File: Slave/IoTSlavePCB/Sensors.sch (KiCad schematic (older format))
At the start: 4 parts, among them U5 SHTC3

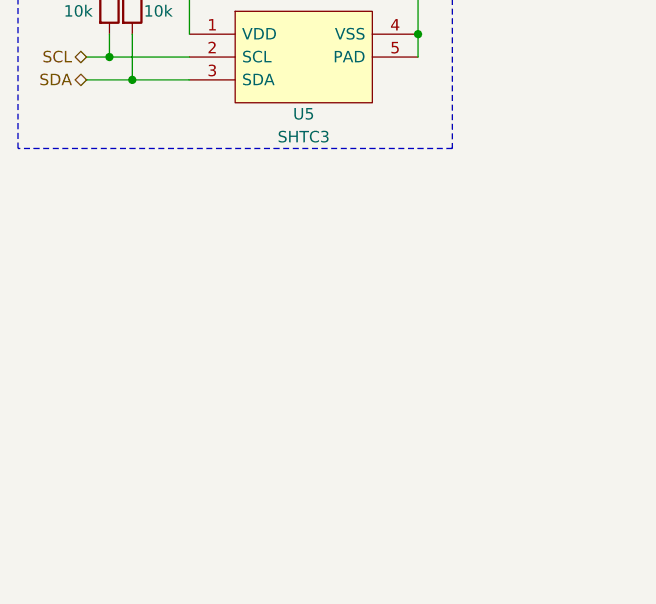
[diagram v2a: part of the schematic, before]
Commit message: Added battery voltage measurement circuit. Optimizations to antenna and general component placement.
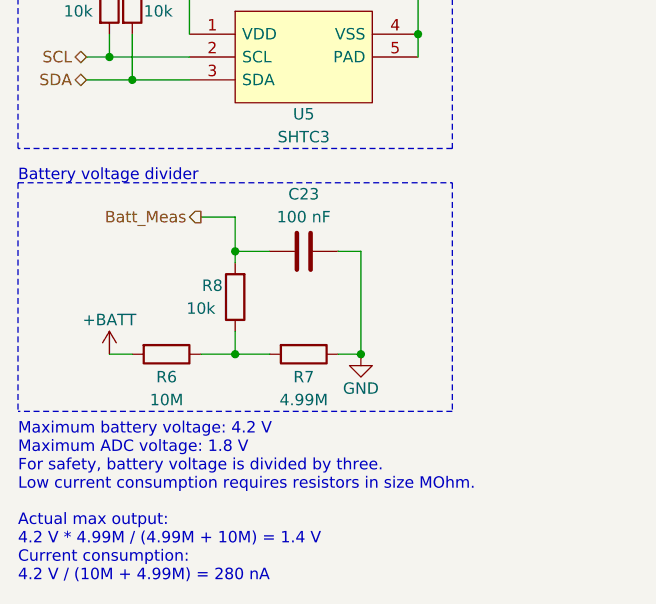
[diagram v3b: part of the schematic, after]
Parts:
- added C23: 100 nF, Capacitor_SMD:C_0603_1608Metric, symbol Device:C
- added R6: 10M, Resistor_SMD:R_0603_1608Metric, symbol Device:R
- added R7: 4.99M, Resistor_SMD:R_0603_1608Metric, symbol Device:R
- added R8: 10k, Resistor_SMD:R_0603_1608Metric, symbol Device:R
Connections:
- net GND: now also C23.1, R7.1
- new net: R6.1, R7.2, R8.1
- new net +BATT: R6.2
- new net Batt_Meas: C23.2, R8.2
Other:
- note added: "Actual max output:\n4.2 V * 4.99M / (4.99M + 10M) = 1.4 V\nCurrent consumption:\n4.2 V / (10M + 4.99M) = 280 nA"
- note added: "Battery voltage divider"
- note added: "Maximum battery voltage: 4.2 V\nMaximum ADC voltage: 1.8 V\nFor safety, battery voltage is divided by three.\nLow current consumption requires resistors in size MOhm."
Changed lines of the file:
@@
 Text Notes 4500 3100 0    50   ~ 0
 Temperature and humidity sensor
+$Comp
+L power:+BATT #PWR063
+U 1 1 5FC228FA
+P 4900 5200
+F 0 "#PWR063" H 4900 5050 50  0001 C CNN
+F 1 "+BATT" H 4900 5350 50  0000 C CNN
+F 2 "" H 4900 5200 50  0001 C CNN
+F 3 "" H 4900 5200 50  0001 C CNN
+	1    4900 5200
+	1    0    0    -1
+$EndComp
+$Comp
+L Device:R R6
+U 1 1 5FC2324E
+P 5150 5200
+F 0 "R6" V 5250 5200 50  0000 C CNN
+F 1 "10M" V 5350 5200 50  0000 C CNN
+F 2 "Resistor_SMD:R_0603_1608Metric" V 5080 5200 50  0001 C CNN
+F 3 "~" H 5150 5200 50  0001 C CNN
+	1    5150 5200
+	0    1    1    0
+$EndComp
+$Comp
+L Device:R R7
+U 1 1 5FC23C04
+P 5750 5200
+F 0 "R7" V 5850 5200 50  0000 C CNN
+F 1 "4.99M" V 5950 5200 50  0000 C CNN
+F 2 "Resistor_SMD:R_0603_1608Metric" V 5680 5200 50  0001 C CNN
+F 3 "~" H 5750 5200 50  0001 C CNN
+	1    5750 5200
+	0    1    1    0
+$EndComp
+Wire Wire Line
+	4900 5200 5000 5200
+Wire Wire Line
+	5900 5200 6000 5200
+$Comp
+L power:GND #PWR064
+U 1 1 5FC257F4
+P 6000 5200
+F 0 "#PWR064" H 6000 4950 50  0001 C CNN
+F 1 "GND" H 6000 5050 50  0000 C CNN
+F 2 "" H 6000 5200 50  0001 C CNN
+F 3 "" H 6000 5200 50  0001 C CNN
+	1    6000 5200
+	1    0    0    -1
+$EndComp
+Text HLabel 5300 4600 0    50   Output ~ 0
+Batt_Meas
+Wire Notes Line
+	4500 4450 6400 4450
+Text Notes 4500 4450 0    50   ~ 0
+Battery voltage divider
+Text Notes 4500 5800 0    50   ~ 0
+Maximum battery voltage: 4.2 V\nMaximum ADC voltage: 1.8 V\nFor safety, battery voltage is divided by three.\nLow current consumption requires resistors in size MOhm.
+Text Notes 4500 6200 0    50   ~ 0
+Actual max output:\n4.2 V * 4.99M / (4.99M + 10M) = 1.4 V\nCurrent consumption:\n4.2 V / (10M + 4.99M) = 280 nA
+$Comp
+L Device:C C23
+U 1 1 5FC33A49
+P 5750 4750
+F 0 "C23" V 5500 4750 50  0000 C CNN
+F 1 "100 nF" V 5600 4750 50  0000 C CNN
+F 2 "Capacitor_SMD:C_0603_1608Metric" H 5788 4600 50  0001 C CNN
+F 3 "~" H 5750 4750 50  0001 C CNN
+	1    5750 4750
+	0    1    1    0
+$EndComp
+Wire Wire Line
+	5450 4600 5450 4750
+Wire Wire Line
+	5450 4750 5600 4750
+Wire Wire Line
+	5900 4750 6000 4750
+Connection ~ 6000 5200
+Wire Wire Line
+	5300 4600 5450 4600
+$Comp
+L Device:R R8
+U 1 1 5FC3819F
+P 5450 4950
+F 0 "R8" H 5550 4900 50  0000 C CNN
+F 1 "10k" H 5600 5000 50  0000 C CNN
+F 2 "Resistor_SMD:R_0603_1608Metric" V 5380 4950 50  0001 C CNN
+F 3 "~" H 5450 4950 50  0001 C CNN
+	1    5450 4950
+	-1   0    0    1
+$EndComp
+Wire Wire Line
+	5300 5200 5450 5200
+Wire Wire Line
+	5450 5100 5450 5200
+Connection ~ 5450 5200
+Wire Wire Line
+	5450 5200 5600 5200
+Connection ~ 5450 4750
+Wire Wire Line
+	5450 4750 5450 4800
+Wire Wire Line
+	6000 4750 6000 5200
+Wire Notes Line
+	6400 5450 4500 5450
+Wire Notes Line
+	6400 4450 6400 5450
+Wire Notes Line
+	4500 4450 4500 5450
 $EndSCHEMATC
